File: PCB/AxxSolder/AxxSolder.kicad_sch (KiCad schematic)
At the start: 93 parts, among them IC1 LTC4440AHMS8E-5#PBF, IC2 STM32G431KBT6, IC3 TMP236AQDBZRQ1, IC4 OPA2333AIDRBR, IC5 STM32G431KBT6, IC6 TPS54302DDCR, J1 Conn_01x07_Male, J4 Conn_01x07_Male, Q2 2N7002NXAKR, U1 PEC11L-4220F-S0015, U2 BSC014N04LS

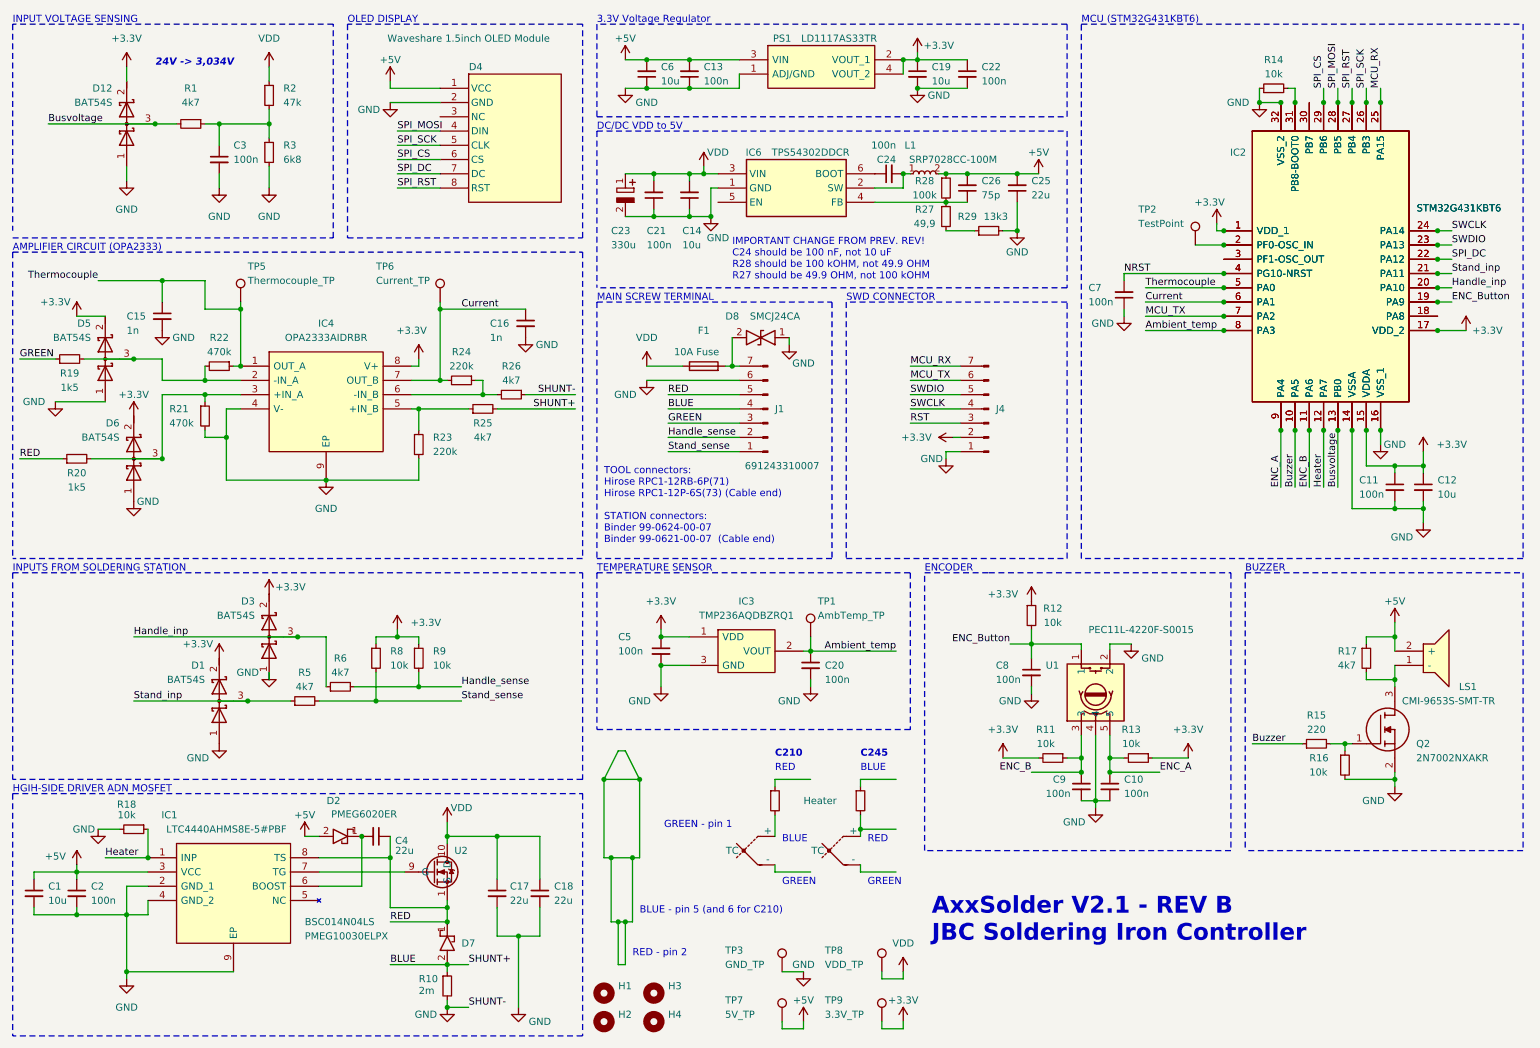
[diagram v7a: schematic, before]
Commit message: Update PCB design to V2.2 - correct fault in 5V DC/DC and change the VDD tVS diode to a 600W instead of 1.5kW and small PCB improvements
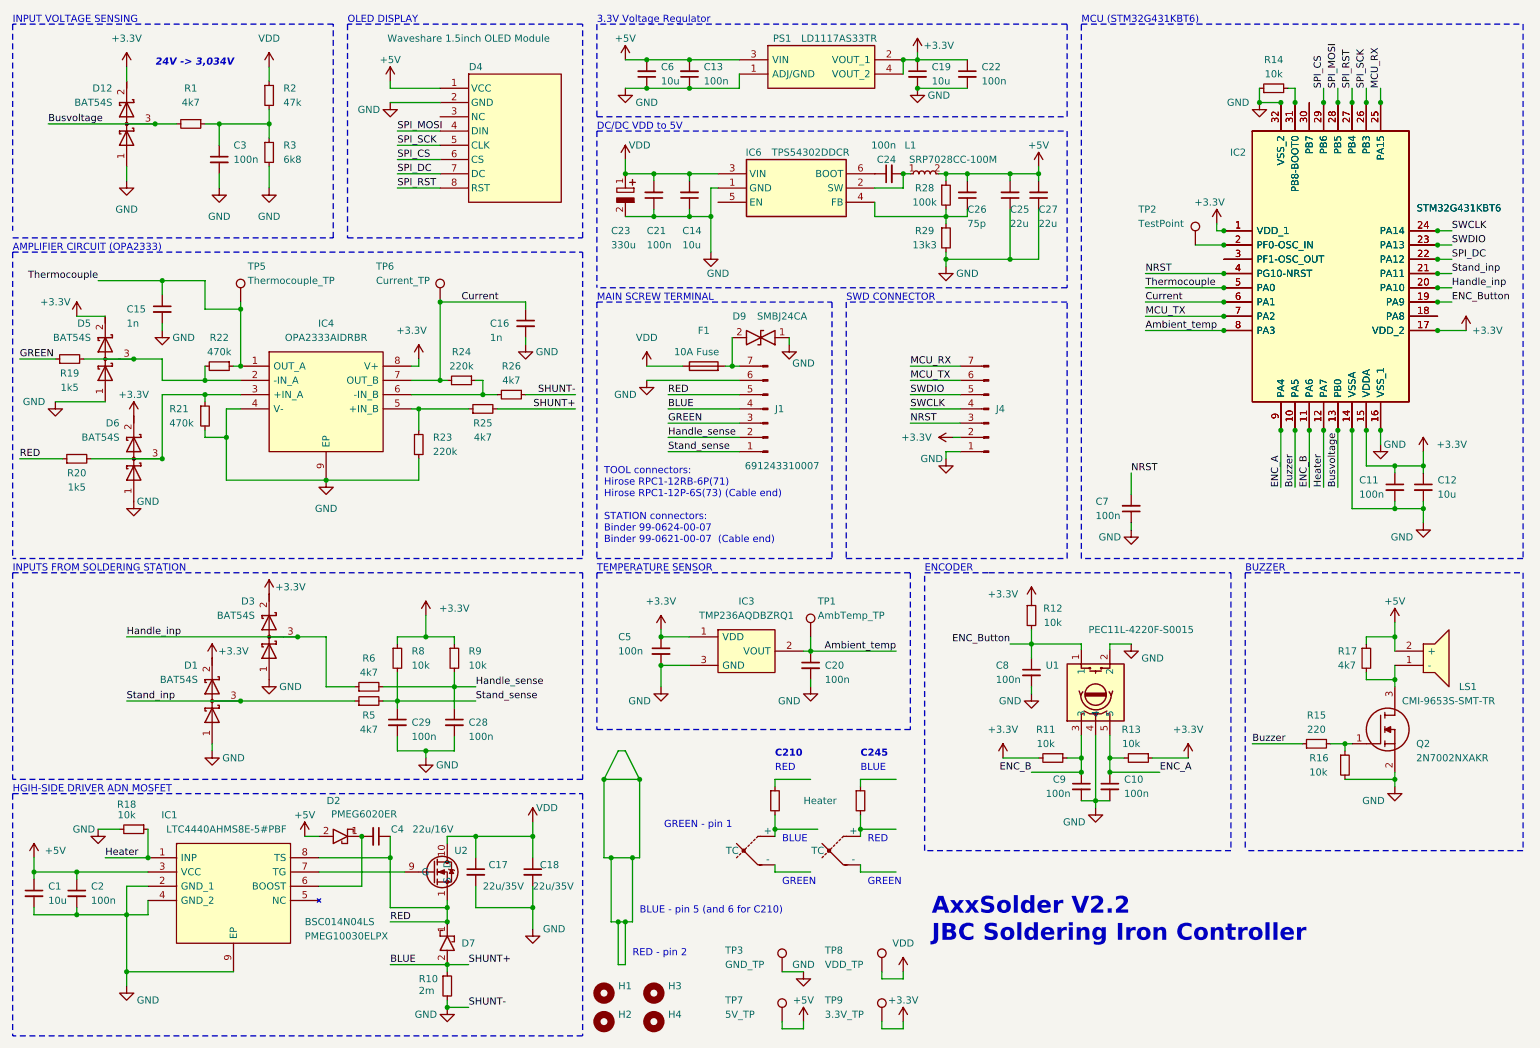
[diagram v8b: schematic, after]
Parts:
- removed D8: SMCJ24CA, SMCJ24CA:DIONM7969X262N, symbol SMCJ24CA:SMCJ24CA
- removed R27: 49,9, Resistor_SMD:R_0805_2012Metric, symbol Device:R_Small
- added C27: 22u, Capacitor_SMD:C_1206_3216Metric, symbol Device:C_Small
- added C28, C29: 100n, Capacitor_SMD:C_0805_2012Metric, symbol Device:C_Small
- added D9: SMBJ24CA, DIOM5436X261N, symbol SMBJ24CA:SMBJ24CA
- C17, C18: value 22u -> 22u/35V
- C25: footprint Capacitor_SMD:C_0805_2012Metric -> Capacitor_SMD:C_1206_3216Metric
- C4: value 22u -> 22u/16V
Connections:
- net RST is gone; now on net NRST: J4.3 (Pin_3)
- net +5V: now also C27.2
- net GND: now also C27.1, C28.2, C29.2, D9.1
- net Handle_sense: now also C28.1
- net Stand_sense: now also C29.1
- net at R29.1: now also C26.1, IC6.4 (FB), R28.2
- net at F1.2, J1.7 (Pin_7): now also D9.2
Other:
- note added: "AxxSolder V2.2 JBC Soldering Iron Controller"
- note removed: "AxxSolder V2.1 - REV B JBC Soldering Iron Controller"
- note removed: "IMPORTANT CHANGE FROM PREV. REV! C24 should be 100 nF, not 10 uF R28 should be 100 kOHM, not 49.9 OHM R27 should be 49.9 OHM, not 100 kOHM"
- moved on the sheet: C15, C17, C18, C25, C26, C7, D1, R28, R29, R5, R6, R8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
